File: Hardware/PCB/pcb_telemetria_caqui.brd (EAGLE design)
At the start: 105.2 x 104.1 mm, 35 parts

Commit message: att
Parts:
- removed TBEAM_LEFT, TBEAM_RIGHT: 61301311121, Headers:61301311121
- added U$1: TTGOBEAM, bibliotecattgo:TTGOBEAM
- moved SL2 83.1 mm to (4.52, 11.0), turned to 270 degrees
- moved R7 82.5 mm to (23.5, 5.19)
- moved R9 82.5 mm to (23.5, 2.65)
- moved R11 81.8 mm to (23.3, 13.5)
- moved R3 81.8 mm to (23.3, 11.0)
- moved R5 81.8 mm to (23.3, 8.46)
- moved R12 81.5 mm to (30.0, 17.4), turned to 90 degrees
- moved SL7 80.1 mm to (4.52, 3.87), turned to 270 degrees
- moved R4 77.2 mm to (33.8, 17.4), turned to 90 degrees
- moved HC4067 73.9 mm to (74.8, 24.5), turned to 0 degrees
- moved R6 73.0 mm to (37.6, 17.4), turned to 270 degrees
- moved R8 69.0 mm to (41.4, 17.4), turned to 90 degrees
- moved R10 65.2 mm to (45.2, 17.4), turned to 270 degrees
- moved C_BAUX 59.6 mm to (97.4, 18.1)
- moved BB_BE_C 51.6 mm to (17.4, 60.6), turned to 0 degrees
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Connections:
- new net GND1: U$1.GND1
- new net GND2: U$1.GND3
- net 0: now also U$1.0; no longer TBEAM_RIGHT.5
- net 13: now also U$1.13; no longer TBEAM_LEFT.4
- net 14: now also U$1.14; no longer TBEAM_LEFT.5
- net 2: now also U$1.2; no longer TBEAM_LEFT.3
- net 21: now also U$1.21; no longer TBEAM_RIGHT.10
- net 22: now also U$1.22; no longer TBEAM_RIGHT.9
- net 23: now also U$1.23; no longer TBEAM_RIGHT.3
- net 25: now also U$1.25; no longer TBEAM_LEFT.6
- net 3.3V: now also U$1.3.3V; no longer TBEAM_RIGHT.11
- net 32: now also U$1.32; no longer TBEAM_LEFT.8
- net 33: now also U$1.33; no longer TBEAM_LEFT.7
- net 34: now also U$1.34; no longer TBEAM_LEFT.10
- net 35: now also U$1.35; no longer TBEAM_LEFT.9
- net 3V3: now also U$1.3V3; no longer TBEAM_RIGHT.7
- net 4: now also U$1.4; no longer TBEAM_RIGHT.4
- net 5V: now also U$1.5V; no longer TBEAM_LEFT.1
- net C0: now also R10.2, R9.1; no longer R3.2, R4.1
- net C1: now also R7.2, R8.1; no longer R5.1, R6.2
- net C2: now also R5.1, R6.2; no longer R7.2, R8.1
- net C3: now also R3.2, R4.1; no longer R10.2, R9.1
- net GND: now also U$1.GND; no longer TBEAM_LEFT.2, TBEAM_RIGHT.6, TBEAM_RIGHT.8
- net LORA1: now also U$1.LORA1; no longer TBEAM_RIGHT.13
- net LORA2: now also U$1.LORA2; no longer TBEAM_RIGHT.12
- net RST: now also U$1.RST; no longer TBEAM_LEFT.11
- net RX: now also U$1.RX; no longer TBEAM_RIGHT.2
- net TX: now also U$1.TX; no longer TBEAM_RIGHT.1
- net VN: now also U$1.VN; no longer TBEAM_LEFT.12
- net VP: now also U$1.VP; no longer TBEAM_LEFT.13
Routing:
- net GND: track 127.0 -> 0.56 mm
- net C4: track 67.0 -> 4.00 mm
- net C5: track 67.6 -> 8.75 mm
- net C6: track 67.2 -> 13.7 mm
- net C7: track 67.4 -> 18.0 mm
- net 22: track 47.9 -> 0.00 mm
- net 21: track 47.9 -> 0.03 mm
- net 14: track 31.0 -> 3.14 mm
- net C0: track 29.3 -> 56.5 mm
- net 13: track 46.1 -> 22.8 mm
- net C1: track 29.4 -> 47.3 mm
- net C2: track 29.9 -> 46.8 mm
- net C3: track 30.4 -> 46.2 mm
- net BTN_CRUZEIRO: track 0.00 -> 15.2 mm
- net DMS_IN: track 0.00 -> 15.0 mm
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
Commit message: uplix
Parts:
- removed BB_BE_C: CURRENT-SENSOR-ACS712, diy-modules:CURRENT-SENSOR-ACS712
- added C_BP: CURRENT-SENSOR-ACS712, diy-modules:CURRENT-SENSOR-ACS712
- added R25, R27: 2.2k, rcl:0204/7
- added R26, R28: 3.9k, rcl:0204/7
- added TEMP: (no value), con-amp-quick:02P
- moved C_BAUX 92.6 mm to (18.1, 65.8), turned to 0 degrees
- moved SHUNTS 21.5 mm to (105.8, 83.9), turned to 270 degrees
- moved R1 5.81 mm to (14.6, 51.5)
- moved R13 5.81 mm to (14.6, 57.2)
- moved R14 5.81 mm to (25.4, 57.2)
- moved R2 5.81 mm to (25.4, 51.5)
- moved SL1 5.81 mm to (4.43, 54.0)
- moved U$1 5.81 mm to (78.7, 91.0)
- moved R15 2.04 mm to (13.3, 22.2)
- moved R17 2.04 mm to (13.3, 24.8)
- moved SL4 2.04 mm to (3.87, 22.2)
- moved SL3 2.04 mm to (3.87, 29.9)
- moved R19 2.04 mm to (13.3, 28.6)
- moved R21 2.04 mm to (13.3, 31.1)
- moved R23 2.04 mm to (13.3, 19.7)
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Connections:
- removed net EN: HC4067.J2.3
- removed net S0: HC4067.J2.4
- removed net S1: HC4067.J2.5
- removed net S2: HC4067.J2.6
- removed net S3: HC4067.J2.7
- removed net SIG: HC4067.J2.8
- removed net VCC: BB_BE_C.1, C_BAUX.1, HC4067.J2.2
- new net N$1: C_BP.2, R25.2
- new net N$2: C_BAUX.2, R27.2
- net 0: now also HC4067.J2.7
- net 13: now also R1.1, R2.2; no longer R23.2, R24.1
- net 14: now also R21.1, R22.2; no longer R13.1, R14.2
- net 2: now also R13.1, R14.2; no longer R11.2, R12.1
- net 21: now also SHUNTS.1; no longer SHUNTS.2
- net 22: now also SHUNTS.2; no longer SHUNTS.1
- net 23: now also HC4067.J2.3
- net 25: now also R11.2, R12.1; no longer R1.1, R2.2
- net 32: now also HC4067.J2.4
- net 33: now also R27.1, R28.1; no longer C_BAUX.2
- net 34: now also HC4067.J2.6
- net 35: now also HC4067.J2.5
- net 4: now also HC4067.J2.8
- net 5V: now also C_BAUX.1, C_BP.1, HC4067.J2.2
- net BAT_AUX: now also R21.2, SL3.1; no longer R23.1, SL4.3
- net C10: now also TEMP.1
- net C4: now also R23.2, R24.1; no longer R21.1, R22.2
- net C5: now also R15.2, R16.1; no longer R19.2, R20.1
- net C7: now also R19.2, R20.1; no longer R15.2, R16.1
- net C8: now also R25.1, R26.1
- net C9: now also TEMP.2
- net COOLER_E: now also R23.1, SL4.3; no longer R21.2, SL3.1
- net GND: now also C_BP.3, R26.2, R28.2; no longer BB_BE_C.3
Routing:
- net 25: track 3.14 -> 176.9 mm
- net 5V: track 0.00 -> 158.6 mm
- net 14: track 3.14 -> 144.2 mm
- net 32: track 0.00 -> 104.7 mm
- net 35: track 0.00 -> 100.5 mm
- net 34: track 0.00 -> 97.3 mm
- net C8: track 0.00 -> 76.4 mm
- net 2: track 2.85 -> 76.4 mm
- net C4: track 4.00 -> 74.6 mm
- net C10: track 0.00 -> 70.4 mm
- net 13: track 22.8 -> 92.5 mm
- net C9: track 0.00 -> 69.4 mm
- net 23: track 0.00 -> 63.4 mm
- net C5: track 8.75 -> 61.7 mm
- net 0: track 0.00 -> 51.1 mm
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- added copper zone on layer 1, net GND
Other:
- board size 105.2 x 104.1 mm -> 117.5 x 115.1 mm

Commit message: up
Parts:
- added IC1: 7805TV, linear:TO220V
- added SUPPLY: (no value), con-amp-quick:02P
- moved SHUNTS 7.77 mm to (106.5, 91.6)
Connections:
- new net VI: IC1.1, SUPPLY.2
- new net VO: IC1.3
- net 3V3: now also HC4067.J2.2
- net 5V: no longer HC4067.J2.2
- net GND: now also IC1.2, SUPPLY.1
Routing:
- net 3V3: track 0.00 -> 97.5 mm
- net 5V: track 158.6 -> 171.4 mm
- net 21: track 36.8 -> 42.0 mm
- net 22: track 33.3 -> 37.5 mm
- net C8: track 76.4 -> 80.4 mm
- removed copper zone on layer 1, net GND

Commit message: Changes in the board and code
mudancas no codigo e placa
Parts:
- added U$2: DC-DC-STEP-DOWN-LM2596, diy-modules:DC-DC-STEP-DOWN-LM2596
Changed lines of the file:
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@@
 <?xml version="1.0" encoding="utf-8"?>
 <!DOCTYPE eagle SYSTEM "eagle.dtd">
-<eagle version="9.5.0">
+<eagle version="9.4.2">
 <drawing>
 <settings>
@@
 <attribute name="VALUE" x="103.2611625" y="59.060078125" size="1.27" layer="27" ratio="10" rot="R270"/>
 </element>
+<element name="U$2" library="diy-modules" package="DC-DC-STEP-DOWN-LM2596" value="DC-DC-STEP-DOWN-LM2596" x="0" y="0" smashed="yes">
+<attribute name="NAME" x="0" y="11.43" size="1.27" layer="25" align="bottom-center"/>
+<attribute name="VALUE" x="0" y="-11.43" size="1.27" layer="27" align="top-center"/>
+</element>
 </elements>

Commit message: ultima att
up
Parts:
- removed U$2: DC-DC-STEP-DOWN-LM2596, diy-modules:DC-DC-STEP-DOWN-LM2596
- added TEMP2: (no value), con-amp-quick:02P
- renumbered TEMP to TEMP1
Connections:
- new net C21: TEMP1.2, TEMP2.2
- new net C22: TEMP1.1, TEMP2.1
- net 13: no longer R1.1, R2.2
- net 14: no longer R21.1, R22.2
- net 2: no longer R13.1, R14.2
- net 25: no longer R11.2, R12.1
- net 33: no longer R27.1, R28.1
- net C10: now also R1.1, R2.2; no longer TEMP1.1
- net C11: now also R11.2, R12.1
- net C12: now also R21.1, R22.2
- net C13: now also R13.1, R14.2
- net C9: now also R27.1, R28.1; no longer TEMP1.2
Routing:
- net 25: track 176.9 -> 0.00 mm
- net 14: track 144.2 -> 0.00 mm
- net 13: track 92.5 -> 0.00 mm
- net 2: track 76.4 -> 0.00 mm
- net C9: track 69.4 -> 0.00 mm
- net C10: track 70.4 -> 3.14 mm
- net 33: track 51.0 -> 0.00 mm
- net 5V: track 171.4 -> 167.3 mm
- net 32: track 104.7 -> 108.1 mm
- net C13: track 0.00 -> 3.14 mm
- net 35: track 100.5 -> 103.5 mm
- net 34: track 97.0 -> 100.0 mm
- net C11: track 0.00 -> 2.85 mm

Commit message: att nos pinos e adicao de regulador pwm
tired
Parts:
- removed IC1: 7805TV, linear:TO220V
- added U$2: DC-DC-STEP-DOWN-LM2596, diy-modules:DC-DC-STEP-DOWN-LM2596
- moved TEMP2 152.4 mm to (105.4, 93.9), turned to 270 degrees
- moved TEMP1 115.5 mm to (105.3, 99.3)
- moved SHUNTS 14.0 mm to (105.2, 105.6)
- moved R28 10.1 mm to (39.2, 61.0), turned to 180 degrees
- moved R27 4.43 mm to (39.1, 65.6), turned to 180 degrees
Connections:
- removed net C21: TEMP1.2, TEMP2.2
- removed net C22: TEMP1.1, TEMP2.1
- removed net VO: IC1.3
- new net VCC: U$2.OUT+
- net 21: now also TEMP1.2, TEMP2.2
- net 22: now also TEMP1.1, TEMP2.1
- net C10: now also R21.1, R22.2; no longer R1.1, R2.2
- net C11: now also R1.1, R2.2; no longer R11.2, R12.1
- net C12: now also R13.1, R14.2; no longer R21.1, R22.2
- net C13: now also R27.1, R28.1; no longer R13.1, R14.2
- net C4: now also R11.2, R12.1; no longer R23.2, R24.1
- net C5: now also R23.2, R24.1; no longer R15.2, R16.1
- net C6: now also R15.2, R16.1; no longer R17.1, R18.2
- net C7: now also R17.1, R18.2; no longer R19.2, R20.1
- net C8: now also R19.2, R20.1; no longer R25.1, R26.1
- net C9: now also R25.1, R26.1; no longer R27.1, R28.1
- net GND: now also U$2.IN-, U$2.OUT-; no longer IC1.2
- net VI: now also U$2.IN+; no longer IC1.1
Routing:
- net C8: track 80.4 -> 0.00 mm
- net C4: track 74.6 -> 0.00 mm
- net C5: track 61.7 -> 0.00 mm
- net C6: track 60.7 -> 0.00 mm
- net C7: track 59.4 -> 0.00 mm
- net C12: track 0.00 -> 58.1 mm
- net C11: track 2.85 -> 57.9 mm
- net C10: track 3.14 -> 57.2 mm
- net C13: track 3.14 -> 40.8 mm
- net 21: track 42.0 -> 72.5 mm
- net 22: track 37.5 -> 53.9 mm
- net 34: track 100.0 -> 94.2 mm
- net N$2: track 9.02 -> 3.30 mm

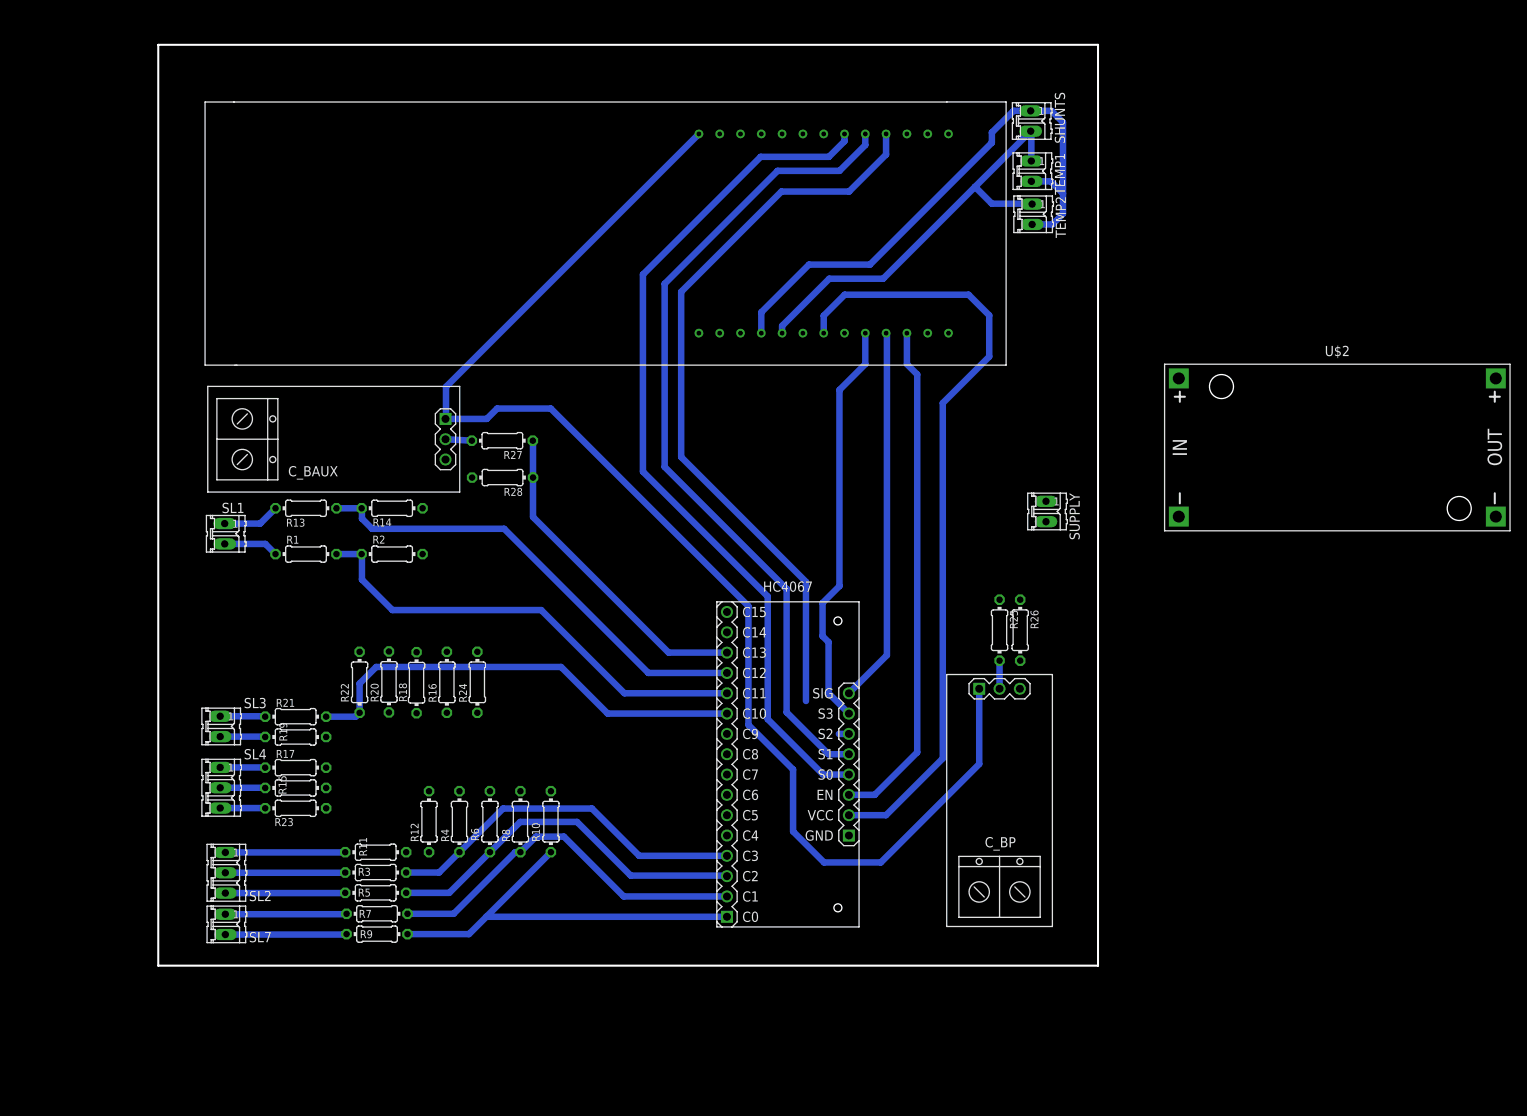
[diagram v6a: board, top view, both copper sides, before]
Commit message: Placa finalizada, aguardando ajustes
Finalizou-se o roteamento pre testes. Aguardando testes para realização de ajustes.
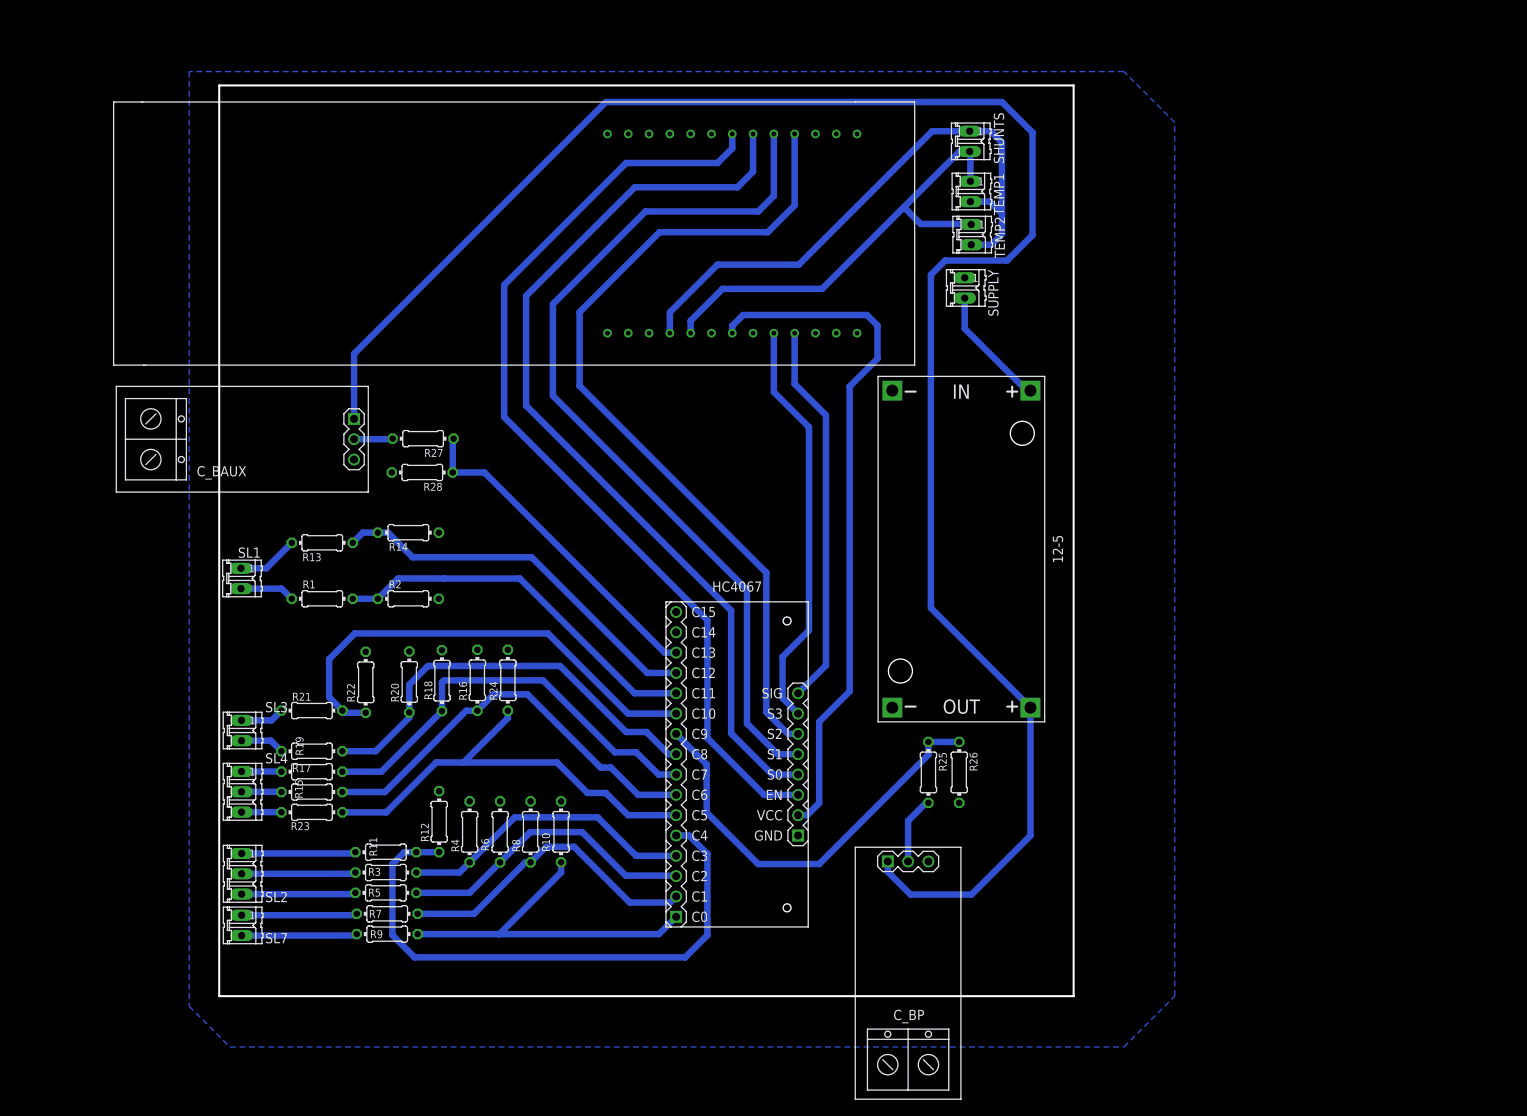
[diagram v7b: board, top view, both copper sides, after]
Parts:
- removed U$2: DC-DC-STEP-DOWN-LM2596, diy-modules:DC-DC-STEP-DOWN-LM2596
- added 12-5: DC-DC-STEP-DOWN-LM2596, diy-modules:DC-DC-STEP-DOWN-LM2596
- moved SUPPLY 29.7 mm to (96.9, 84.7)
- moved C_BP 24.4 mm to (89.9, -0.94)
- moved R25 19.9 mm to (92.4, 24.2)
- moved R26 19.3 mm to (96.3, 24.2)
- moved U$1 11.4 mm to (67.3, 91.0)
- moved C_BAUX 11.4 mm to (6.63, 65.8)
- moved R28 10.1 mm to (29.1, 61.6)
- moved R27 9.91 mm to (29.2, 65.9)
- moved TEMP1 8.03 mm to (97.6, 96.8)
- moved SHUNTS 8.03 mm to (97.6, 103.0)
- moved TEMP2 8.03 mm to (97.7, 91.4)
- moved HC4067 6.35 mm to (68.5, 25.2)
- moved R1 5.95 mm to (16.6, 45.9)
- moved R2 5.95 mm to (27.4, 45.9)
- moved SL1 5.95 mm to (6.47, 48.4)
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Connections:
- net 23: no longer HC4067.J2.3
- net 33: now also HC4067.J2.3
- net 5V: no longer C_BAUX.1, C_BP.1
- net GND: now also 12-5.IN-, 12-5.OUT-; no longer U$2.IN-, U$2.OUT-
- net VCC: now also 12-5.OUT+, C_BAUX.1, C_BP.1; no longer U$2.OUT+
- net VI: now also 12-5.IN+; no longer U$2.IN+
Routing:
- net VCC: track 0.00 -> 233.7 mm
- net 5V: track 167.3 -> 0.00 mm
- net 33: track 0.00 -> 118.8 mm
- net C4: track 0.00 -> 72.0 mm
- net 23: track 63.7 -> 0.00 mm
- net C5: track 0.00 -> 55.8 mm
- net C7: track 0.00 -> 53.4 mm
- net C8: track 0.00 -> 53.1 mm
- net C9: track 0.00 -> 52.9 mm
- net C6: track 0.00 -> 52.0 mm
- net VI: track 0.00 -> 15.2 mm
- net 34: track 94.2 -> 106.1 mm
- net 3V3: track 97.5 -> 86.1 mm
- net C11: track 57.9 -> 47.4 mm
- net C12: track 58.1 -> 48.2 mm
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- added copper zone on layer 16, net GND
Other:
- board size 117.5 x 115.1 mm -> 106.8 x 113.8 mm
